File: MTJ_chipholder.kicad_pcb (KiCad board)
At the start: 4 copper layers, 74 x 35.5 mm, 3 parts, among them J1 8428-21B1-RK-TR

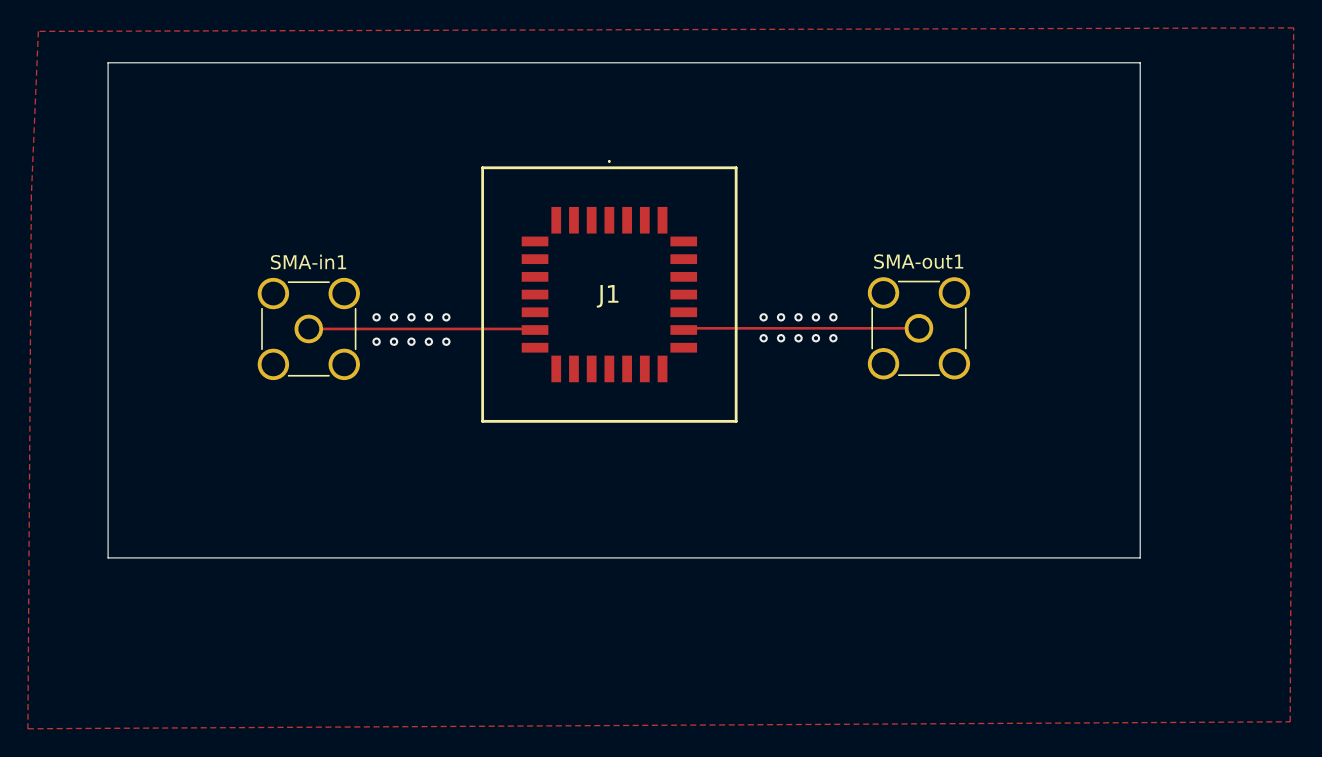
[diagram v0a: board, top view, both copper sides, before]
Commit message: - use 0.3 mm for the track width, corresponding to JLCPCB JLC04161H-7628, with 0.2mm clearance from ground on each side (coplanar waveguide) - added a few more gnd vias (they can/should also be under the chip holder) - put gnd planes on all layers
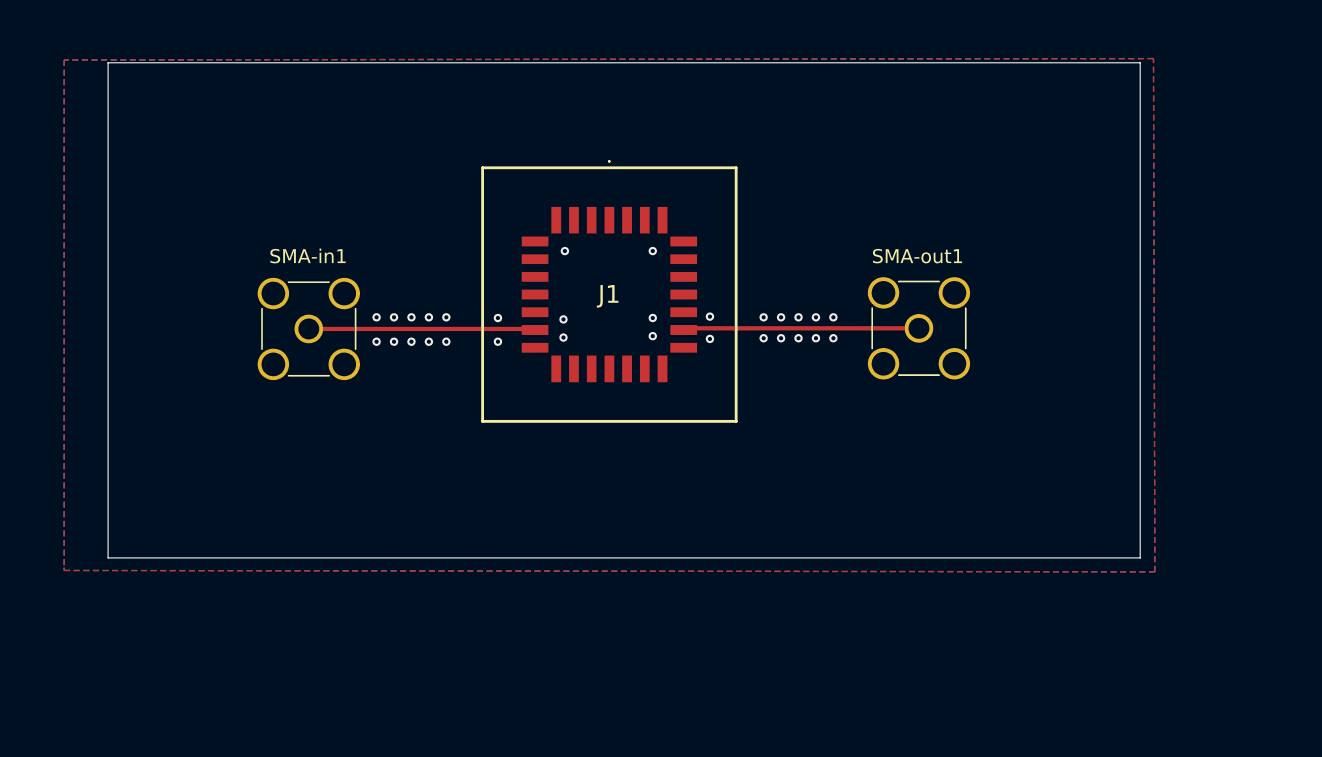
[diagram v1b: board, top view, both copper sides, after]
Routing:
- net GND: vias 20 -> 30
- added copper zone on B.Cu, net GND
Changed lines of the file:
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@@
 		)
 		(fp_text user "${REFERENCE}"
-			(at 0 0 0)
+			(at 0.01 -12.22 0)
 			(layer "F.Fab")
 			(effects
@@
 		(tags "SMA THT Female Jack Vertical")
 		(property "Reference" "SMA-in1"
-			(at 0 -4.75 0)
+			(at -0.04 -5.185 0)
 			(layer "F.SilkS")
 			(effects
@@
 			(at 0 5 0)
 			(layer "F.Fab")
+			(hide yes)
 			(effects
 				(font
@@
 			(fill no)
 			(layer "F.Fab")
-		)
-		(fp_text user "${REFERENCE}"
-			(at 0 0 0)
-			(layer "F.Fab")
-			(effects
-				(font
-					(size 1 1)
-					(thickness 0.15)
-				)
-			)
 		)
 		(pad "1" thru_hole circle
@@
 		(tags "SMA THT Female Jack Vertical")
 		(property "Reference" "SMA-out1"
-			(at 0 -4.75 0)
+			(at -0.085 -5.14 0)
 			(layer "F.SilkS")
 			(effects
@@
 			(at 0 5 0)
 			(layer "F.Fab")
+			(hide yes)
 			(effects
 				(font
@@
 			(fill no)
 			(layer "F.Fab")
-		)
-		(fp_text user "${REFERENCE}"
-			(at -0.15 -0.75 0)
-			(layer "F.Fab")
-			(effects
-				(font
-					(size 1 1)
-					(thickness 0.15)
-				)
-			)
 		)
 		(pad "1" thru_hole circle
@@
 		(start 88.64 88.085)
 		(end 104.785 88.085)
-		(width 0.19)
+		(width 0.3)
 		(layer "F.Cu")
 		(net 23)
@@
 	)
 	(via
+		(at 107 82.5)
+		(size 0.6)
+		(drill 0.3)
+		(layers "F.Cu" "B.Cu")
+		(free yes)
+		(net 24)
+	)
+	(via
 		(at 93.5 89)
 		(size 0.6)
@@
 	)
 	(via
+		(at 106.9 88.7)
+		(size 0.6)
+		(drill 0.3)
+		(layers "F.Cu" "B.Cu")
+		(free yes)
+		(net 24)
+	)
+	(via
+		(at 113.3 82.5)
+		(size 0.6)
+		(drill 0.3)
+		(layers "F.Cu" "B.Cu")
+		(free yes)
+		(net 24)
+	)
+	(via
 		(at 122.5 87.25)
 		(size 0.6)
@@
 	)
 	(via
+		(at 102.2 87.3)
+		(size 0.6)
+		(drill 0.3)
+		(layers "F.Cu" "B.Cu")
+		(free yes)
+		(net 24)
+	)
+	(via
 		(at 94.75 87.25)
 		(size 0.6)
@@
 	)
 	(via
+		(at 106.9 87.4)
+		(size 0.6)
+		(drill 0.3)
+		(layers "F.Cu" "B.Cu")
+		(free yes)
+		(net 24)
+	)
+	(via
 		(at 123.75 87.25)
 		(size 0.6)
@@
 	)
 	(via
+		(at 102.2 89)
+		(size 0.6)
+		(drill 0.3)
+		(layers "F.Cu" "B.Cu")
+		(free yes)
+		(net 24)
+	)
+	(via
 		(at 126.25 87.25)
 		(size 0.6)
@@
 	)
 	(via
+		(at 113.3 87.3)
+		(size 0.6)
+		(drill 0.3)
+		(layers "F.Cu" "B.Cu")
+		(free yes)
+		(net 24)
+	)
+	(via
 		(at 122.5 88.75)
 		(size 0.6)
@@
 	)
 	(via
+		(at 117.4 87.2)
+		(size 0.6)
+		(drill 0.3)
+		(layers "F.Cu" "B.Cu")
+		(free yes)
+		(net 24)
+	)
+	(via
 		(at 123.75 88.75)
 		(size 0.6)
@@
 	)
 	(via
+		(at 117.4 88.8)
+		(size 0.6)
+		(drill 0.3)
+		(layers "F.Cu" "B.Cu")
+		(free yes)
+		(net 24)
+	)
+	(via
 		(at 98.5 87.25)
+		(size 0.6)
+		(drill 0.3)
+		(layers "F.Cu" "B.Cu")
+		(free yes)
+		(net 24)
+	)
+	(via
+		(at 113.3 88.6)
 		(size 0.6)
 		(drill 0.3)
@@
 		(start 132.385 88.04)
 		(end 115.64 88.04)
-		(width 0.19)
+		(width 0.3)
 		(layer "F.Cu")
 		(net 25)
@@
 		(net 24)
 		(net_name "GND")
-		(layer "F.Cu")
+		(layers "F.Cu" "B.Cu" "In1.Cu" "In2.Cu")
 		(name "gndplane")
 		(hatch edge 0.5)
 		(priority 1)
 		(connect_pads
-			(clearance 0.15)
+			(clearance 0.2)
 		)
 		(min_thickness 0.25)
@@
 		(polygon
 			(pts
-				(xy 68.75 78.5) (xy 68.5 116.75) (xy 159 116.25) (xy 159.25 66.5) (xy 69.25 66.75)
-			)
-		)
-	)
-	(zone
-		(net 24)
-		(net_name "GND")
-		(layers "In1.Cu" "In2.Cu")
-		(name "gndplane")
-		(hatch edge 0.5)
-		(connect_pads
-			(clearance 0.15)
-		)
-		(min_thickness 0.25)
-		(filled_areas_thickness no)
-		(fill yes
-			(thermal_gap 0.5)
-			(thermal_bridge_width 0.5)
-			(island_removal_mode 1)
-			(island_area_min 10)
-		)
-		(polygon
-			(pts
-				(xy 55.25 54) (xy 55.35 146.4) (xy 192.65 147) (xy 191.95 54)
-			)
-		)
+				(xy 71.1 105.2) (xy 71.1 105.4) (xy 149.3 105.5) (xy 149.2 68.7) (xy 71.1 68.8)
+			)
+		)
